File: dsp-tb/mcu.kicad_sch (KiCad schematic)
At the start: 26 parts, among them J2 Conn_ARM_SWD_TagConnect_TC2030, U1 STM32H723ZGTx, U5 D3V3XA4B10LP

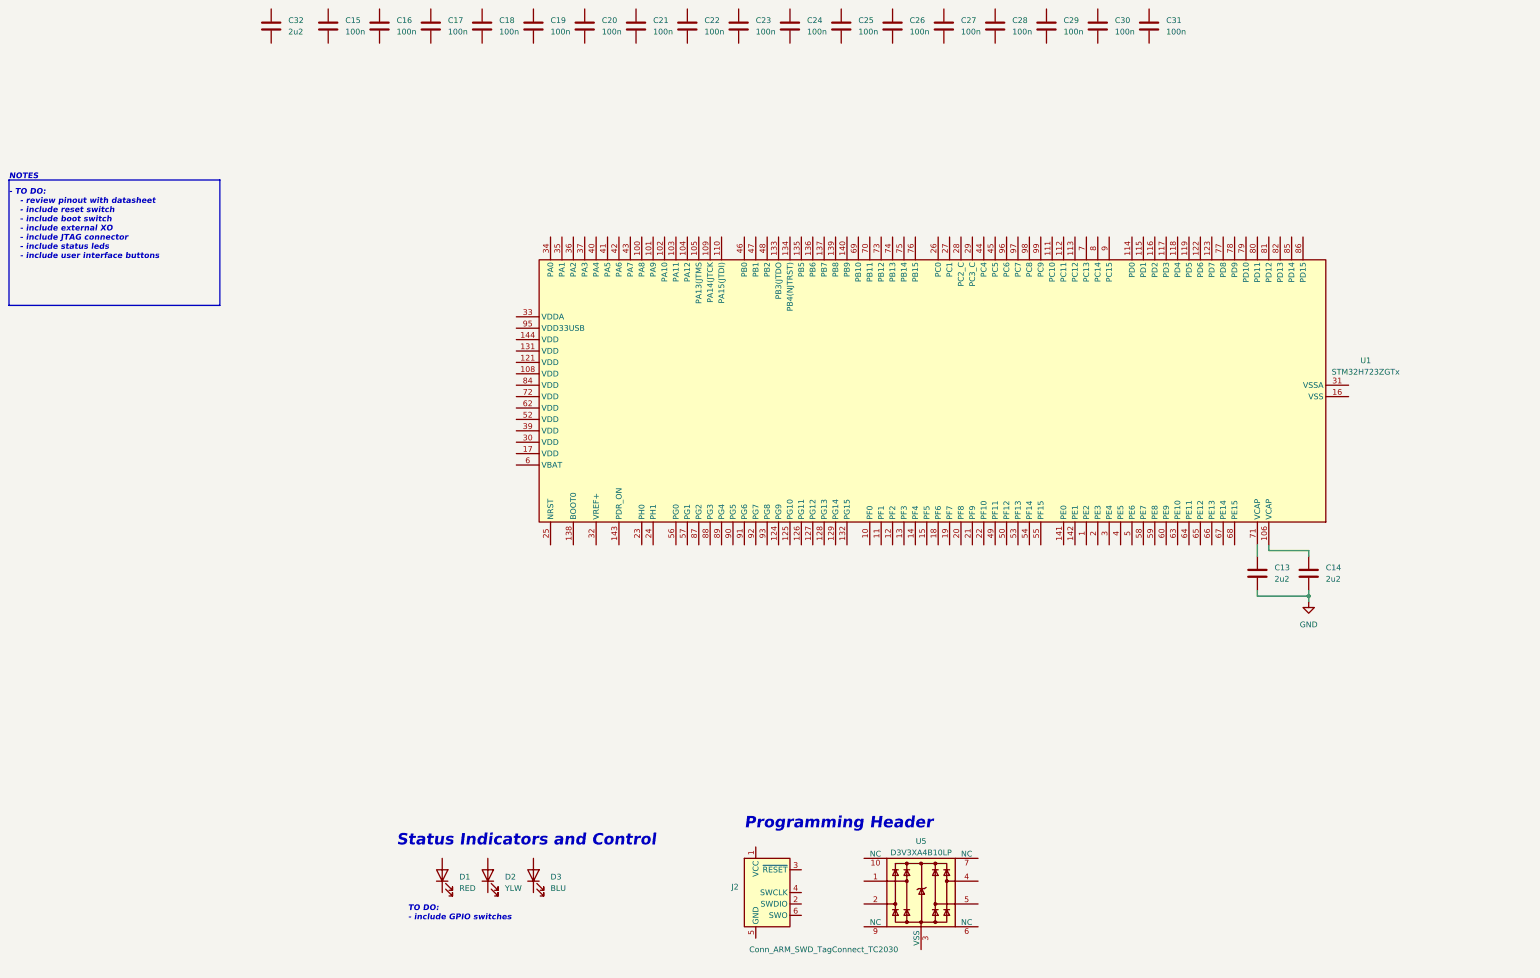
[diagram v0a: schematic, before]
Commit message: dsp: boot0 and reset switches
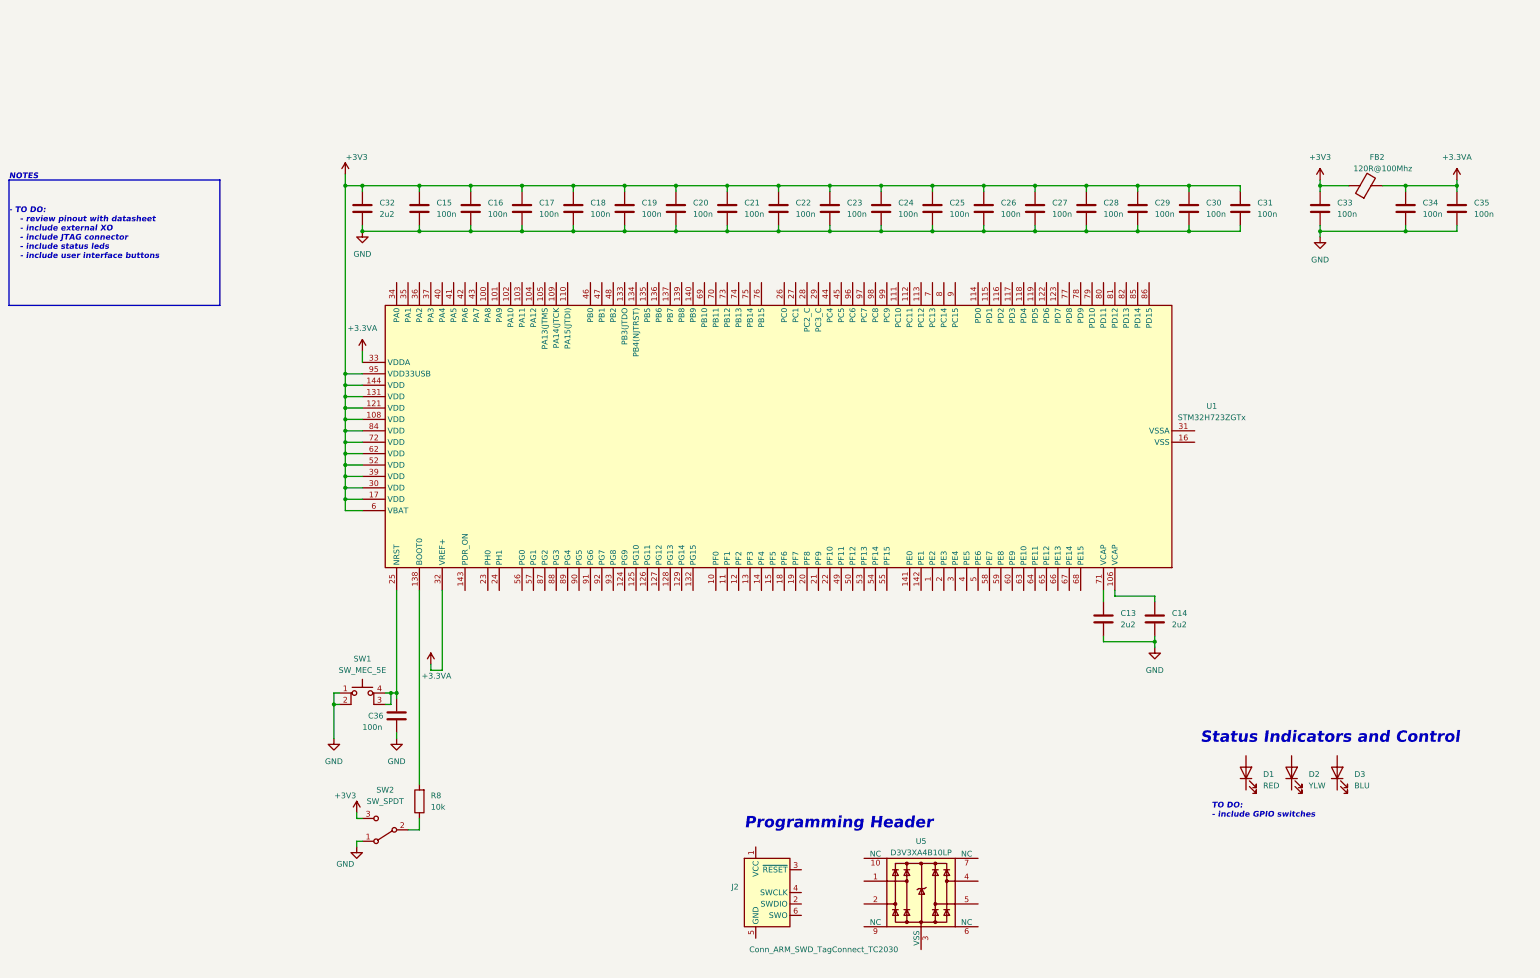
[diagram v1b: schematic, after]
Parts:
- added C33, C34, C35, C36: 100n, Capacitor_SMD:C_0402_1005Metric, symbol Device:C
- added FB2: 120R@100Mhz, Inductor_SMD:L_0402_1005Metric, symbol Device:FerriteBead
- added R8: 10k, Resistor_SMD:R_0402_1005Metric, symbol Device:R
- added SW1: SW_MEC_5E, footprints:PTS645SL43SMTR92LFS_CNK, symbol Switch:SW_MEC_5E
- added SW2: SW_SPDT, footprints:CSS-1210TB_NDC, symbol Switch:SW_SPDT
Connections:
- net GND: now also C15.2, C16.2, C17.2, C18.2, C19.2, C20.2, C21.2, C22.2, C23.2, C24.2, C25.2, C26.2, C27.2, C28.2, C29.2, C30.2, C31.2, C32.2, C33.2, C34.2, C35.2, C36.1, SW1.1, SW1.2, SW2.1 (A)
- net +3V3: now reaches C21.1
- net +3V3: now also C15.1, C16.1, C17.1, C18.1, C19.1, C20.1, C22.1, C23.1, C24.1, C25.1, C26.1, C27.1, C28.1, C29.1, C30.1, C31.1, C32.1, U1.108 (VDD), U1.121 (VDD), U1.131 (VDD), U1.144 (VDD), U1.17 (VDD), U1.30 (VDD), U1.39 (VDD), U1.52 (VDD), U1.6 (VBAT), U1.62 (VDD), U1.72 (VDD), U1.84 (VDD), U1.95 (VDD33USB), C33.1, FB2.1, SW2.3 (C)
- net at U1.138 (BOOT0): now also R8.2
- net at U1.25 (NRST): now also C36.2, SW1.3 (K), SW1.4 (A)
- net +3.3VA: now reaches U1.32 (VREF+)
- net +3.3VA: now also U1.33 (VDDA), C34.1, C35.1, FB2.2
- new net: R8.1, SW2.2 (B)
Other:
- note added: "- TO DO: - review pinout with datasheet - include external XO - include JTAG connector - include status leds - include user interface buttons"
- note removed: "- TO DO: - review pinout with datasheet - include reset switch - include boot switch - include external XO - include JTAG connector - include status leds - include user interface buttons"
- moved on the sheet: C13, C14, C15, C16, C17, C18, C19, C20, C21, C22, C23, C24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

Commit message: dsp-tb: finish schematic drawings
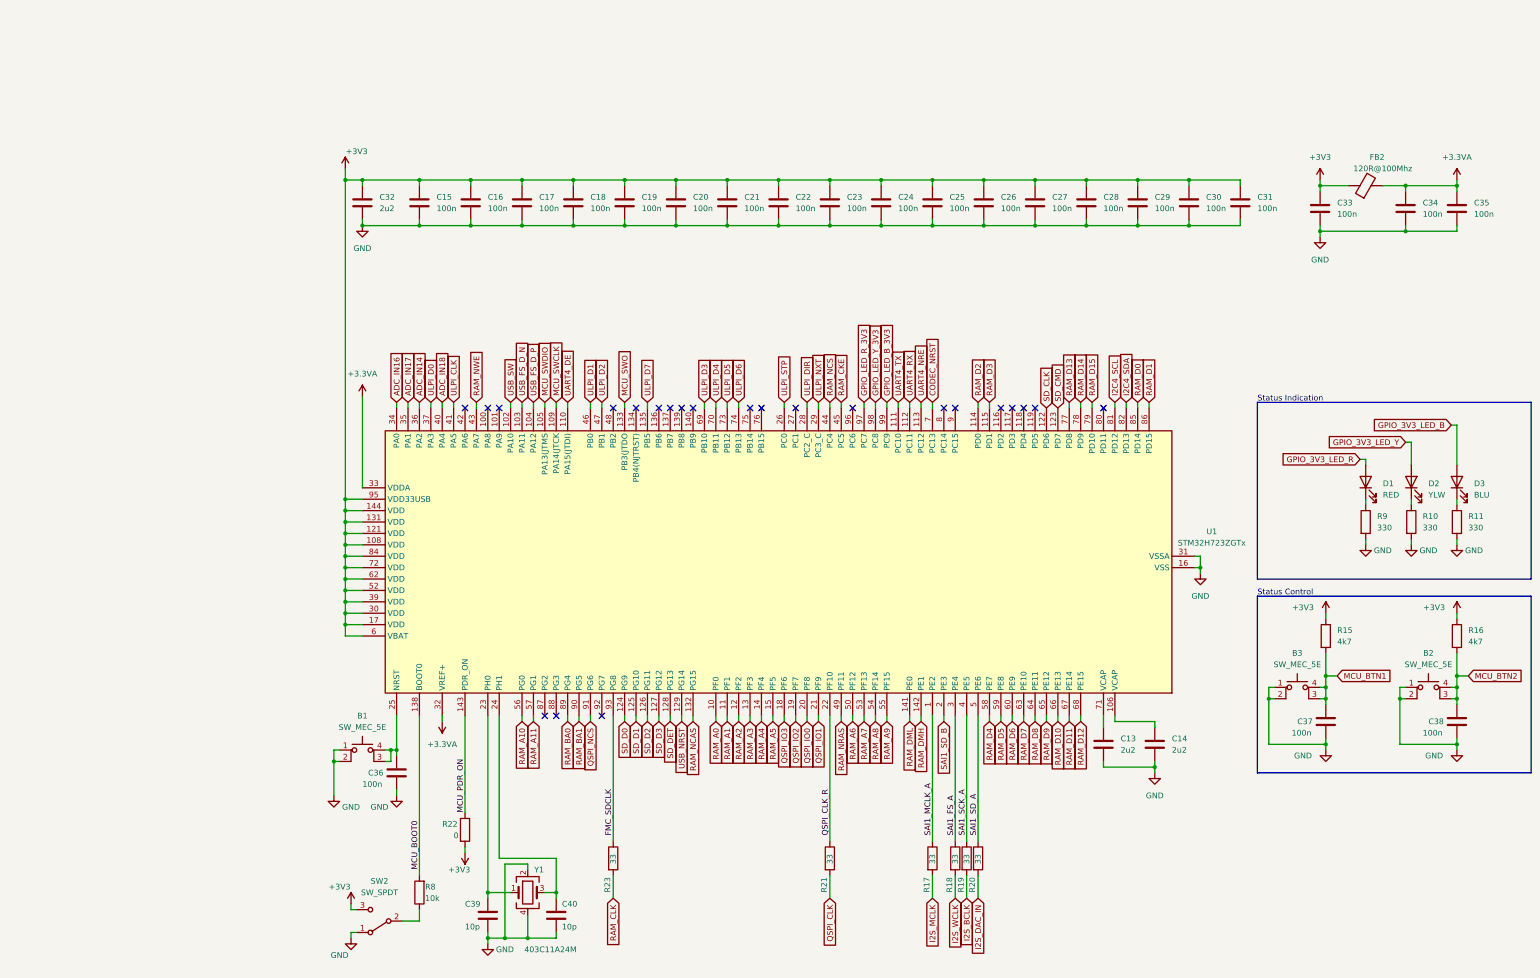
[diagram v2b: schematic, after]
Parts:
- removed J2: Conn_ARM_SWD_TagConnect_TC2030, Connector:Tag-Connect_TC2030-IDC-FP_2x03_P1.27mm_Vertical, symbol Connector:Conn_ARM_SWD_TagConnect_TC2030
- removed U5: D3V3XA4B10LP, Package_DFN_QFN:Diodes_UDFN-10_1.0x2.5mm_P0.5mm, symbol Power_Protection:D3V3XA4B10LP
- added B2, B3: SW_MEC_5E, footprints:PTS645SL43SMTR92LFS_CNK, symbol Switch:SW_MEC_5E
- added C37, C38: 100n, Capacitor_SMD:C_0402_1005Metric, symbol Device:C
- added C39, C40: 10p, Capacitor_SMD:C_0402_1005Metric, symbol Device:C
- added R10, R11, R9: 330, Resistor_SMD:R_0402_1005Metric, symbol Device:R
- added R15, R16: 4k7, Resistor_SMD:R_0402_1005Metric, symbol Device:R
- added R17, R18, R19, R20, R21, R23: 33, Resistor_SMD:R_0402_1005Metric, symbol Device:R
- added R22: 0, Resistor_SMD:R_0402_1005Metric, symbol Device:R
- added Y1: 403C11A24M, Crystal:Crystal_SMD_3225-4Pin_3.2x2.5mm, symbol Device:Crystal_GND24
- renumbered SW1 to B1
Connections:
- net +3V3: now also R15.1, R16.1, R22.2
- net GND: now also U1.107 (VSS), U1.120 (VSS), U1.130 (VSS), U1.16 (VSS), U1.31 (VSSA), U1.38 (VSS), U1.51 (VSS), U1.61 (VSS), U1.83 (VSS), U1.94 (VSS), B2.1, B2.2, B3.1, B3.2, C37.1, C38.1, C39.1, C40.1, R10.2, R11.2, R9.2, Y1.2, Y1.4
- net at D2.1 (K): now also R10.1
- net GPIO_3V3_LED_Y: now reaches D2.2 (A)
- net at D3.1 (K): now also R11.1
- net GPIO_3V3_LED_B: now reaches D3.2 (A)
- net SAI1_MCLK_A: now reaches U1.1 (PE2)
- net SAI1_MCLK_A: now also R17.1
- net RAM_A0: now reaches U1.10 (PF0)
- net USB_SW: now reaches U1.102 (PA10)
- net USB_FS_D_N: now reaches U1.103 (PA11)
- net USB_FS_D_P: now reaches U1.104 (PA12)
- net MCU_SWDIO: now reaches U1.105 (PA13(JTMS)
- net MCU_SWCLK: now reaches U1.109 (PA14(JTCK)
- net RAM_A1: now reaches U1.11 (PF1)
- net UART4_DE: now reaches U1.110 (PA15(JTDI))
- net UART4_TX: now reaches U1.111 (PC10)
- net UART4_RX: now reaches U1.112 (PC11)
- net UART4_NRE: now reaches U1.113 (PC12)
- net RAM_D2: now reaches U1.114 (PD0)
- net RAM_D3: now reaches U1.115 (PD1)
- net RAM_A2: now reaches U1.12 (PF2)
- net SD_CLK: now reaches U1.122 (PD6)
- net SD_CMD: now reaches U1.123 (PD7)
- net SD_D0: now reaches U1.124 (PG9)
- net SD_D1: now reaches U1.125 (PG10)
- net SD_D2: now reaches U1.126 (PG11)
- net SD_D3: now reaches U1.127 (PG12)
- net SD_DET: now reaches U1.128 (PG13)
- net USB_NRST: now reaches U1.129 (PG14)
- net RAM_A3: now reaches U1.13 (PF3)
- net RAM_NCAS: now reaches U1.132 (PG15)
- net MCU_SWO: now reaches U1.133 (PB3(JTDO)
- net ULPI_D7: now reaches U1.135 (PB5)
- net MCU_BOOT0: now reaches R8.2, U1.138 (BOOT0)
- net RAM_A4: now reaches U1.14 (PF4)
- net RAM_DML: now reaches U1.141 (PE0)
- net RAM_DMH: now reaches U1.142 (PE1)
- net MCU_PDR_ON: now reaches U1.143 (PDR_ON)
- net MCU_PDR_ON: now also R22.1
- net RAM_A5: now reaches U1.15 (PF5)
- net QSPI_IO3: now reaches U1.18 (PF6)
- net QSPI_IO2: now reaches U1.19 (PF7)
- net SAI1_SD_B: now reaches U1.2 (PE3)
- net QSPI_IO0: now reaches U1.20 (PF8)
- net QSPI_IO1: now reaches U1.21 (PF9)
- net QSPI_CLK_R: now reaches U1.22 (PF10)
- net QSPI_CLK_R: now also R21.1
- net at U1.23 (PH0): now also C39.2, Y1.1
- net at U1.24 (PH1): now also C40.2, Y1.3
- net ULPI_STP: now reaches U1.26 (PC0)
- net ULPI_DIR: now reaches U1.28 (PC2_C)
- net ULPI_NXT: now reaches U1.29 (PC3_C)
- net SAI1_FS_A: now reaches U1.3 (PE4)
- net SAI1_FS_A: now also R18.1
- net ADC_IN16: now reaches U1.34 (PA0)
- net ADC_IN17: now reaches U1.35 (PA1)
- net ADC_IN14: now reaches U1.36 (PA2)
- net ULPI_D0: now reaches U1.37 (PA3)
- net SAI1_SCK_A: now reaches U1.4 (PE5)
- net SAI1_SCK_A: now also R19.1
- net ADC_IN18: now reaches U1.40 (PA4)
- net ULPI_CLK: now reaches U1.41 (PA5)
- net RAM_NWE: now reaches U1.43 (PA7)
- net RAM_NCS: now reaches U1.44 (PC4)
- net RAM_CKE: now reaches U1.45 (PC5)
- net ULPI_D1: now reaches U1.46 (PB0)
- net ULPI_D2: now reaches U1.47 (PB1)
- net RAM_NRAS: now reaches U1.49 (PF11)
- net SAI1_SD_A: now reaches U1.5 (PE6)
- net SAI1_SD_A: now also R20.1
- net RAM_A6: now reaches U1.50 (PF12)
- net RAM_A7: now reaches U1.53 (PF13)
- net RAM_A8: now reaches U1.54 (PF14)
- net RAM_A9: now reaches U1.55 (PF15)
- net RAM_A10: now reaches U1.56 (PG0)
- net RAM_A11: now reaches U1.57 (PG1)
- net RAM_D4: now reaches U1.58 (PE7)
- net RAM_D5: now reaches U1.59 (PE8)
- net RAM_D6: now reaches U1.60 (PE9)
- net RAM_D7: now reaches U1.63 (PE10)
- net RAM_D8: now reaches U1.64 (PE11)
- net RAM_D9: now reaches U1.65 (PE12)
- net RAM_D10: now reaches U1.66 (PE13)
- net RAM_D11: now reaches U1.67 (PE14)
- net RAM_D12: now reaches U1.68 (PE15)
- net ULPI_D3: now reaches U1.69 (PB10)
- net CODEC_NRST: now reaches U1.7 (PC13)
- net ULPI_D4: now reaches U1.70 (PB11)
- net ULPI_D5: now reaches U1.73 (PB12)
- net ULPI_D6: now reaches U1.74 (PB13)
- net RAM_D13: now reaches U1.77 (PD8)
- net RAM_D14: now reaches U1.78 (PD9)
- net RAM_D15: now reaches U1.79 (PD10)
- net I2C4_SCL: now reaches U1.81 (PD12)
- net I2C4_SDA: now reaches U1.82 (PD13)
- net RAM_D0: now reaches U1.85 (PD14)
- net RAM_D1: now reaches U1.86 (PD15)
- net RAM_BA0: now reaches U1.89 (PG4)
- net RAM_BA1: now reaches U1.90 (PG5)
- net QSPI_NCS: now reaches U1.91 (PG6)
- net FMC_SDCLK: now reaches U1.93 (PG8)
- net FMC_SDCLK: now also R23.1
- net GPIO_LED_R_3V3: now reaches U1.97 (PC7)
- net GPIO_LED_Y_3V3: now reaches U1.98 (PC8)
- net GPIO_LED_B_3V3: now reaches U1.99 (PC9)
- net at D1.1 (K): now also R9.1
- net GPIO_3V3_LED_R: now reaches D1.2 (A)
- new net I2S_BCLK: R19.2
- new net I2S_DAC_IN: R20.2
- new net I2S_MCLK: R17.2
- new net I2S_WCLK: R18.2
- new net MCU_BTN1: B3.3 (K), B3.4 (A), C37.2, R15.2
- new net MCU_BTN2: B2.3 (K), B2.4 (A), C38.2, R16.2
- new net QSPI_CLK: R21.2
- new net RAM_CLK: R23.2
- no-connect marks 0 -> 23
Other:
- note added: "Status Control"
- note added: "Status Indication"
- note removed: "- TO DO: - review pinout with datasheet - include external XO - include JTAG connector - include status leds - include user interface buttons"
- note removed: "NOTES"
- note removed: "Programming Header"
- note removed: "Status Indicators and Control"
- note removed: "TO DO: - include GPIO switches"
- moved on the sheet: B1, C13, C14, C15, C16, C17, C18, C19, C20, C21, C22, C23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
